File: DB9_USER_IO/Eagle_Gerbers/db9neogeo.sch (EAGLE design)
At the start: 14 parts, among them IC1 74HC597D, IC2 74HC597D, IC3 74HC597D

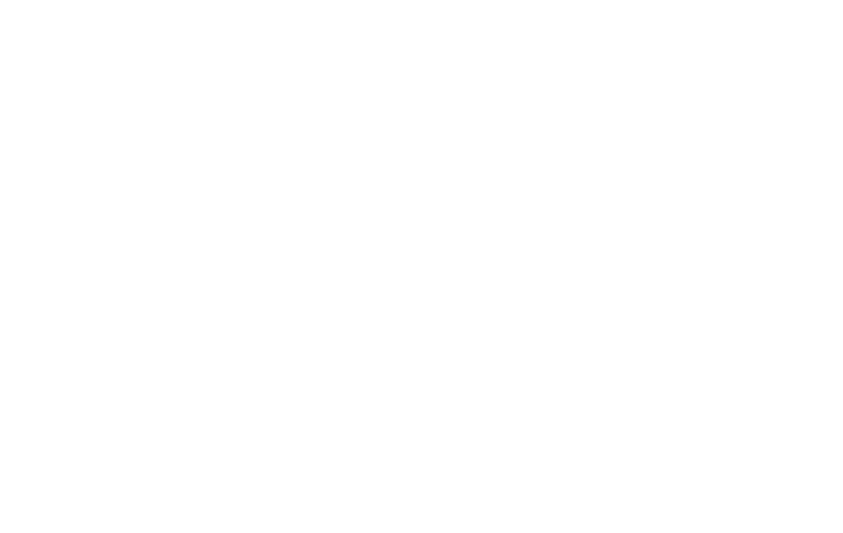
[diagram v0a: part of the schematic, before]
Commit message: updated db9neogeo with usb3 input. added db9neogeo
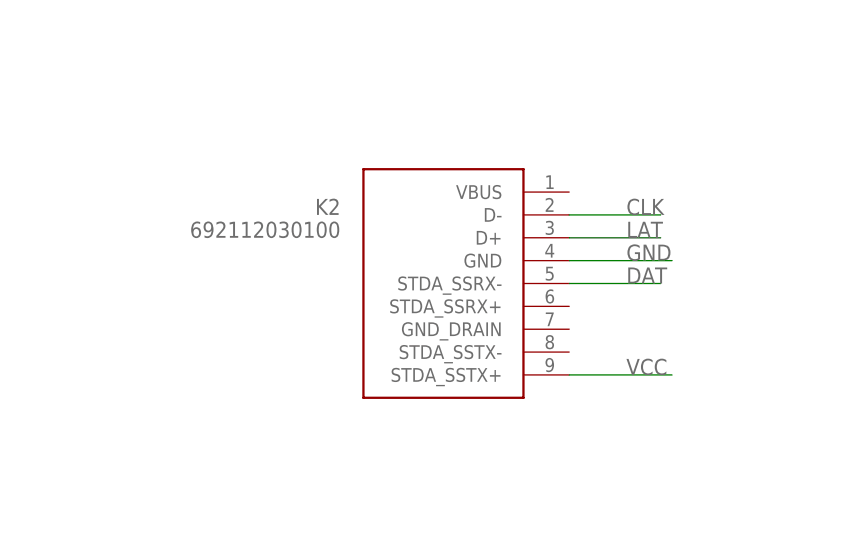
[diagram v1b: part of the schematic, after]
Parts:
- added K2: 692112030100, Wuerth_Elektronik_eiCan_Communication_Connectors_STENCIL:692112030100
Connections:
- net CLK: now also K2.D-
- net DAT: now also K2.STDA_SSRX-
- net GND: now also K2.GND
- net LAT: now also K2.D+
- net VCC: now also K2.STDA_SSTX+
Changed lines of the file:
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@@
 <part name="C2" library="rcl" deviceset="C-EU" device="C0603K" value="100nF"/>
 <part name="C1" library="rcl" deviceset="C-EU" device="C0603K" value="100nF"/>
+<part name="K2" library="Wuerth_Elektronik_eiCan_Communication_Connectors_STENCIL" deviceset="692112030100" device=""/>
 </parts>
 <sheets>
@@
 <instance part="C2" gate="G$1" x="-6.35" y="15.24"/>
 <instance part="C1" gate="G$1" x="-16.51" y="15.24"/>
+<instance part="K2" gate="G$1" x="50.8" y="-27.94" rot="MR0"/>
 </instances>
 <busses>
@@
 <label x="-81.28" y="-44.45" size="1.778" layer="95"/>
 </segment>
+<segment>
+<pinref part="K2" gate="G$1" pin="D-"/>
+<wire x1="63.5" y1="-25.4" x2="73.66" y2="-25.4" width="0.1524" layer="91"/>
+<label x="69.85" y="-25.4" size="1.778" layer="95"/>
+</segment>
 </net>
 <net name="DAT" class="0">
@@
 <wire x1="-45.72" y1="-16.51" x2="-33.02" y2="-16.51" width="0.1524" layer="91"/>
 <label x="-43.18" y="-16.51" size="1.778" layer="95"/>
+</segment>
+<segment>
+<pinref part="K2" gate="G$1" pin="STDA_SSRX-"/>
+<wire x1="63.5" y1="-33.02" x2="73.66" y2="-33.02" width="0.1524" layer="91"/>
+<label x="69.85" y="-33.02" size="1.778" layer="95"/>
 </segment>
 </net>
@@
 <wire x1="-16.51" y1="6.35" x2="-6.35" y2="6.35" width="0.1524" layer="91"/>
 <label x="-13.97" y="3.81" size="1.778" layer="95"/>
+</segment>
+<segment>
+<pinref part="K2" gate="G$1" pin="GND"/>
+<wire x1="63.5" y1="-30.48" x2="74.93" y2="-30.48" width="0.1524" layer="91"/>
+<label x="69.85" y="-30.48" size="1.778" layer="95"/>
 </segment>
 </net>
@@
 <wire x1="-73.66" y1="-52.07" x2="-81.28" y2="-52.07" width="0.1524" layer="91"/>
 <label x="-81.28" y="-52.07" size="1.778" layer="95"/>
+</segment>
+<segment>
+<pinref part="K2" gate="G$1" pin="D+"/>
+<wire x1="63.5" y1="-27.94" x2="73.66" y2="-27.94" width="0.1524" layer="91"/>
+<label x="69.85" y="-27.94" size="1.778" layer="95"/>
 </segment>
 </net>
@@
 <label x="-13.97" y="22.86" size="1.778" layer="95"/>
 </segment>
-</net>
+<segment>
+<pinref part="K2" gate="G$1" pin="STDA_SSTX+"/>
+<wire x1="63.5" y1="-43.18" x2="74.93" y2="-43.18" width="0.1524" layer="91"/>
+<label x="69.85" y="-43.18" size="1.778" layer="95"/>
+</segment>
+</net>
